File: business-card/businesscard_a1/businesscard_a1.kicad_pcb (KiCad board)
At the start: 2 copper layers, 85.6 x 54 mm, 12 parts, among them P1 NFC, P2 CREDIT_CARD, U1 NTAG_NT3H1X01

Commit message: Minor mods
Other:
- net class Default: clearance 0.2 -> 0.195
- rule trace_clearance: 0.2 -> 0.195
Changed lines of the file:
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@@
     (links 23)
     (no_connects 0)
-    (area 105.049999 70.049999 190.750001 124.150001)
+    (area 104.4329 66.4 196.480953 124.150001)
     (thickness 0.6)
     (drawings 14)
@@
   )
   (setup
-    (last_trace_width 0.3)
+    (last_trace_width 0.2)
     (user_trace_width 0.2)
     (user_trace_width 0.3)
     (user_trace_width 0.4)
     (user_trace_width 0.5)
-    (trace_clearance 0.2)
+    (trace_clearance 0.195)
     (zone_clearance 0.508)
     (zone_45_only yes)
@@
   (net 9 /LB)
   (net_class Default "This is the default net class."
-    (clearance 0.2)
+    (clearance 0.195)
     (trace_width 0.2)
     (via_dia 0.7)

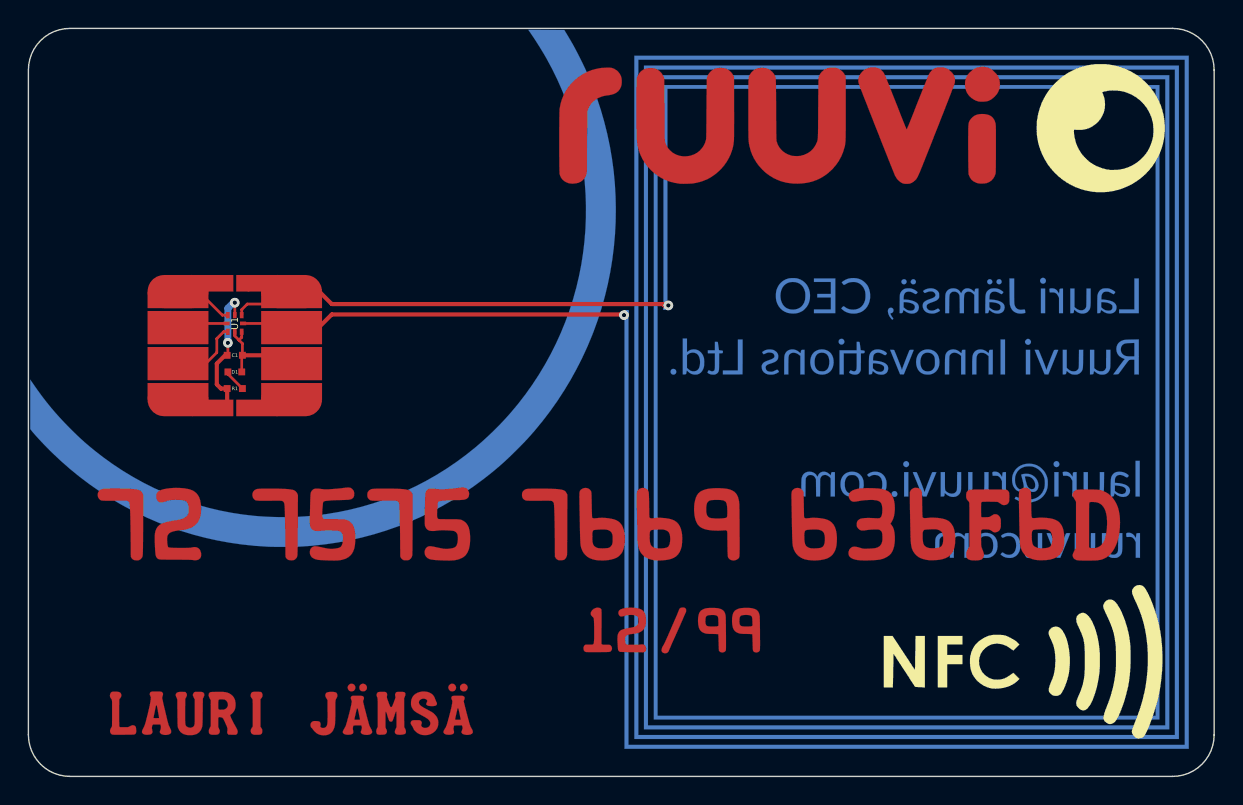
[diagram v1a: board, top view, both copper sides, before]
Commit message: Add copper into the eye
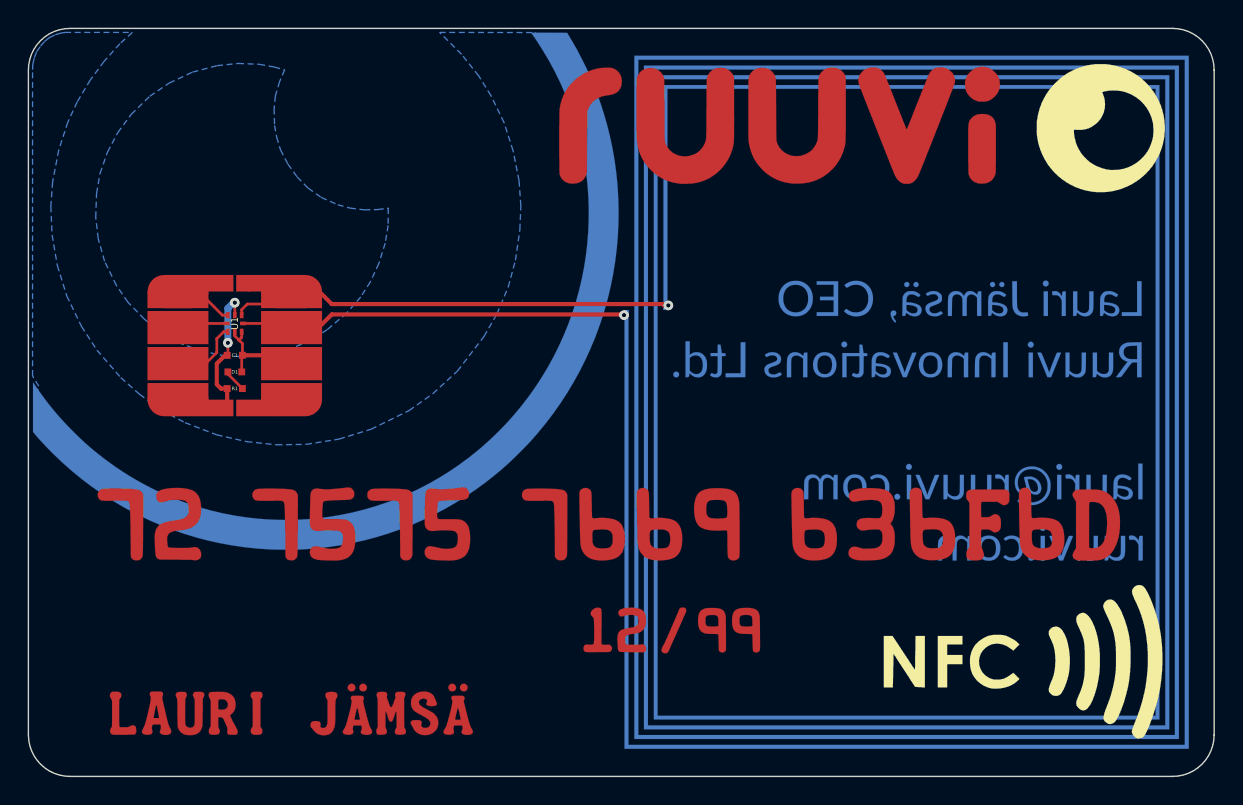
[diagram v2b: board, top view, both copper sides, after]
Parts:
- moved G*** 0.31 mm to (123.7, 85.0)
- moved G*** 0.28 mm to (145.5, 89.5)
- moved G*** 0.28 mm to (145.2, 89.2)
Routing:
- added copper zone on B.Cu, net (none)
- added copper zone on B.Cu, net GND
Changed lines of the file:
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@@
-(kicad_pcb (version 4) (host pcbnew 4.0.1-stable)
+(kicad_pcb (version 4) (host pcbnew "(2016-01-28 BZR 6518)-product")
   (general
     (links 23)
     (no_connects 0)
-    (area 104.4329 66.4 196.480953 124.150001)
+    (area 105.049999 70.049999 190.750001 124.150001)
     (thickness 0.6)
     (drawings 14)
@@
     (34 B.Paste user)
     (35 F.Paste user)
-    (36 B.SilkS user hide)
+    (36 B.SilkS user)
     (37 F.SilkS user)
     (38 B.Mask user)
@@
     (user_trace_width 0.5)
     (trace_clearance 0.195)
-    (zone_clearance 0.508)
-    (zone_45_only yes)
+    (zone_clearance 0.2)
+    (zone_45_only no)
     (trace_min 0.2)
     (segment_width 0.1)
@@
   )
   (module business-card:BUSINESS_BOT_COP (layer B.Cu)
-    (at 145.29 89.27 180)
+    (at 145.49 89.47 180)
     (fp_text reference G*** (at 0 0 180) (layer B.SilkS) hide
       (effects (font (thickness 0.3)) (justify mirror))
@@
   )
   (module business-card:BUSINESS_BOT_MASK (layer B.Cu)
-    (at 145 89 180)
+    (at 145.2 89.2 180)
     (solder_mask_margin 0.2)
     (fp_text reference G*** (at 0 0 180) (layer B.SilkS) hide
@@
   )
   (module business-card:BUSINESS_BOT_SILK (layer B.Cu)
-    (at 124 85 180)
+    (at 123.69 85 180)
     (fp_text reference G*** (at 0 0 180) (layer B.SilkS) hide
       (effects (font (thickness 0.3)) (justify mirror))
@@
       )
     )
+  )
+  (zone (net 1) (net_name GND) (layer B.Cu) (hatch edge 0.508)
+    (connect_pads (clearance 0.3))
+    (min_thickness 0.3)
+    (fill yes (arc_segments 32) (thermal_gap 0.3) (thermal_bridge_width 0.31))
+    (polygon
+      (pts
+        (xy 131.08 83.07) (xy 131.07 84.32) (xy 130.86 85.6) (xy 130.4 87.07) (xy 129.79 88.39)
+        (xy 129.09 89.49) (xy 128.08 90.65) (xy 126.68 91.84) (xy 125.46 92.63) (xy 124.07 93.21)
+        (xy 122.47 93.63) (xy 121.03 93.8) (xy 119.35 93.76) (xy 117.61 93.39) (xy 116.3 92.93)
+        (xy 114.9 92.2) (xy 113.47 91.09) (xy 112.28 89.86) (xy 111.45 88.65) (xy 110.6 86.91)
+        (xy 110.14 85.28) (xy 109.96 83.74) (xy 110.02 82.02) (xy 110.27 80.57) (xy 110.81 79.03)
+        (xy 111.55 77.63) (xy 112.52 76.31) (xy 113.86 75) (xy 115.26 74.05) (xy 116.94 73.26)
+        (xy 118.72 72.79) (xy 120.23 72.63) (xy 121.76 72.69) (xy 122.85 72.89) (xy 123.6 73.09)
+        (xy 123.24 73.93) (xy 122.93 74.97) (xy 122.84 75.88) (xy 122.87 77.1) (xy 123.02 77.94)
+        (xy 123.3 78.87) (xy 123.83 79.89) (xy 124.5 80.82) (xy 125.29 81.63) (xy 126.24 82.3)
+        (xy 127.43 82.83) (xy 128.31 83.07) (xy 129.35 83.2) (xy 130.32 83.18)
+      )
+    )
+  )
+  (zone (net 0) (net_name "") (layer B.Cu) (hatch edge 0.508)
+    (connect_pads (clearance 0.2))
+    (min_thickness 0.2)
+    (fill yes (arc_segments 32) (thermal_gap 0.2) (thermal_bridge_width 0.21))
+    (polygon
+      (pts
+        (xy 111.71 71.2) (xy 110.57 72.47) (xy 109.57 73.82) (xy 108.62 75.41) (xy 107.95 76.86)
+        (xy 107.29 78.88) (xy 106.85 81.17) (xy 106.72 82.94) (xy 106.81 85.01) (xy 107.19 87.22)
+        (xy 107.87 89.41) (xy 108.93 91.61) (xy 110.05 93.33) (xy 111.77 95.31) (xy 113.12 96.51)
+        (xy 114.7 97.66) (xy 116.41 98.56) (xy 118.69 99.44) (xy 120.84 99.93) (xy 123.01 100.16)
+        (xy 125.14 100.13) (xy 127.52 99.75) (xy 129.83 99.04) (xy 132.58 97.69) (xy 134.3 96.47)
+        (xy 136.07 94.84) (xy 137.99 92.34) (xy 138.92 90.72) (xy 139.74 88.77) (xy 140.26 86.84)
+        (xy 140.58 84.63) (xy 140.65 82.91) (xy 140.52 81.09) (xy 140.09 78.93) (xy 139.44 76.9)
+        (xy 138.49 74.95) (xy 137.61 73.53) (xy 136.37 71.97) (xy 134.79 70.39) (xy 141.68 70.4)
+        (xy 142.258779 71.266144) (xy 142.89 71.11) (xy 145.57 76.42) (xy 146.49 83.99) (xy 145.29 91.34)
+        (xy 141.12 98.57) (xy 135.2 103.46) (xy 126.26 106.4) (xy 117.43 105.89) (xy 111.62 103.18)
+        (xy 105.81 97.9) (xy 105.522027 96.428135) (xy 105.68 96.55) (xy 105.85 95.93) (xy 105.4 95.189231)
+        (xy 105.4 73.08) (xy 105.42 72.67) (xy 105.53 72.21) (xy 105.7 71.78) (xy 105.98 71.38)
+        (xy 106.28 71.03) (xy 106.61 70.77) (xy 107.04 70.56) (xy 107.212966 70.501034) (xy 107.49 70.43)
+        (xy 107.75 70.39) (xy 112.61 70.39) (xy 111.71 71.2)
+      )
+    )
